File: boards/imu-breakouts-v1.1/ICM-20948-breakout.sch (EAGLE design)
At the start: 10 parts, among them U1 NCP161, U2 ICM-20948

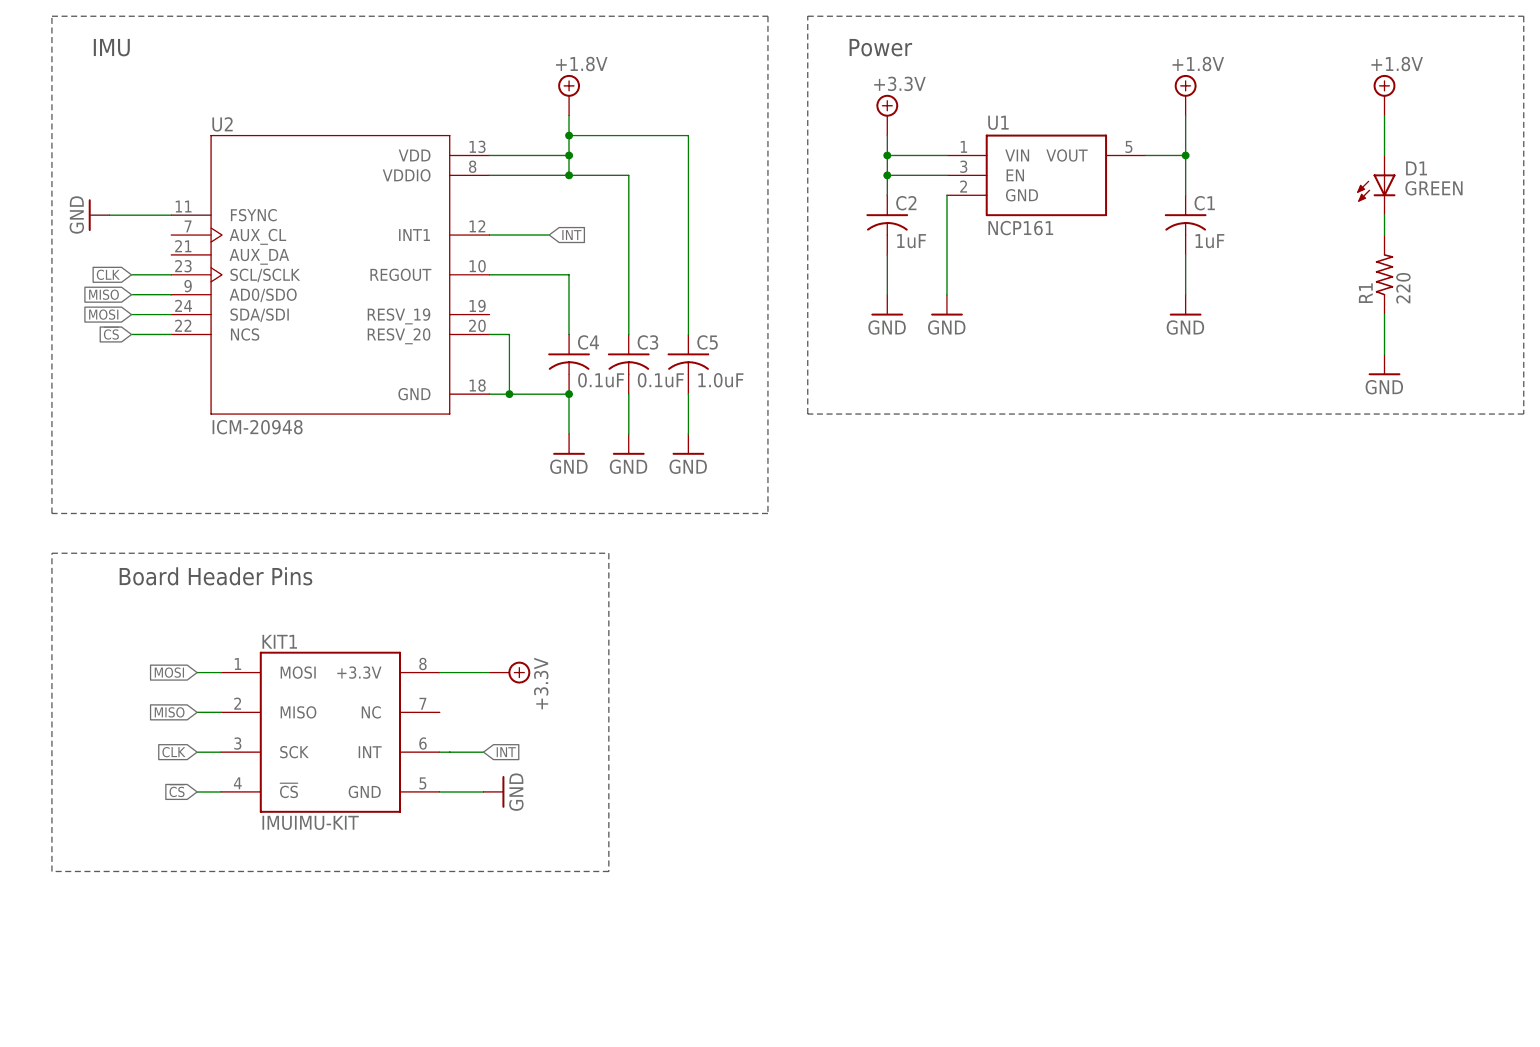
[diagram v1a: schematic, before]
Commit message: Fixed git file locations and version
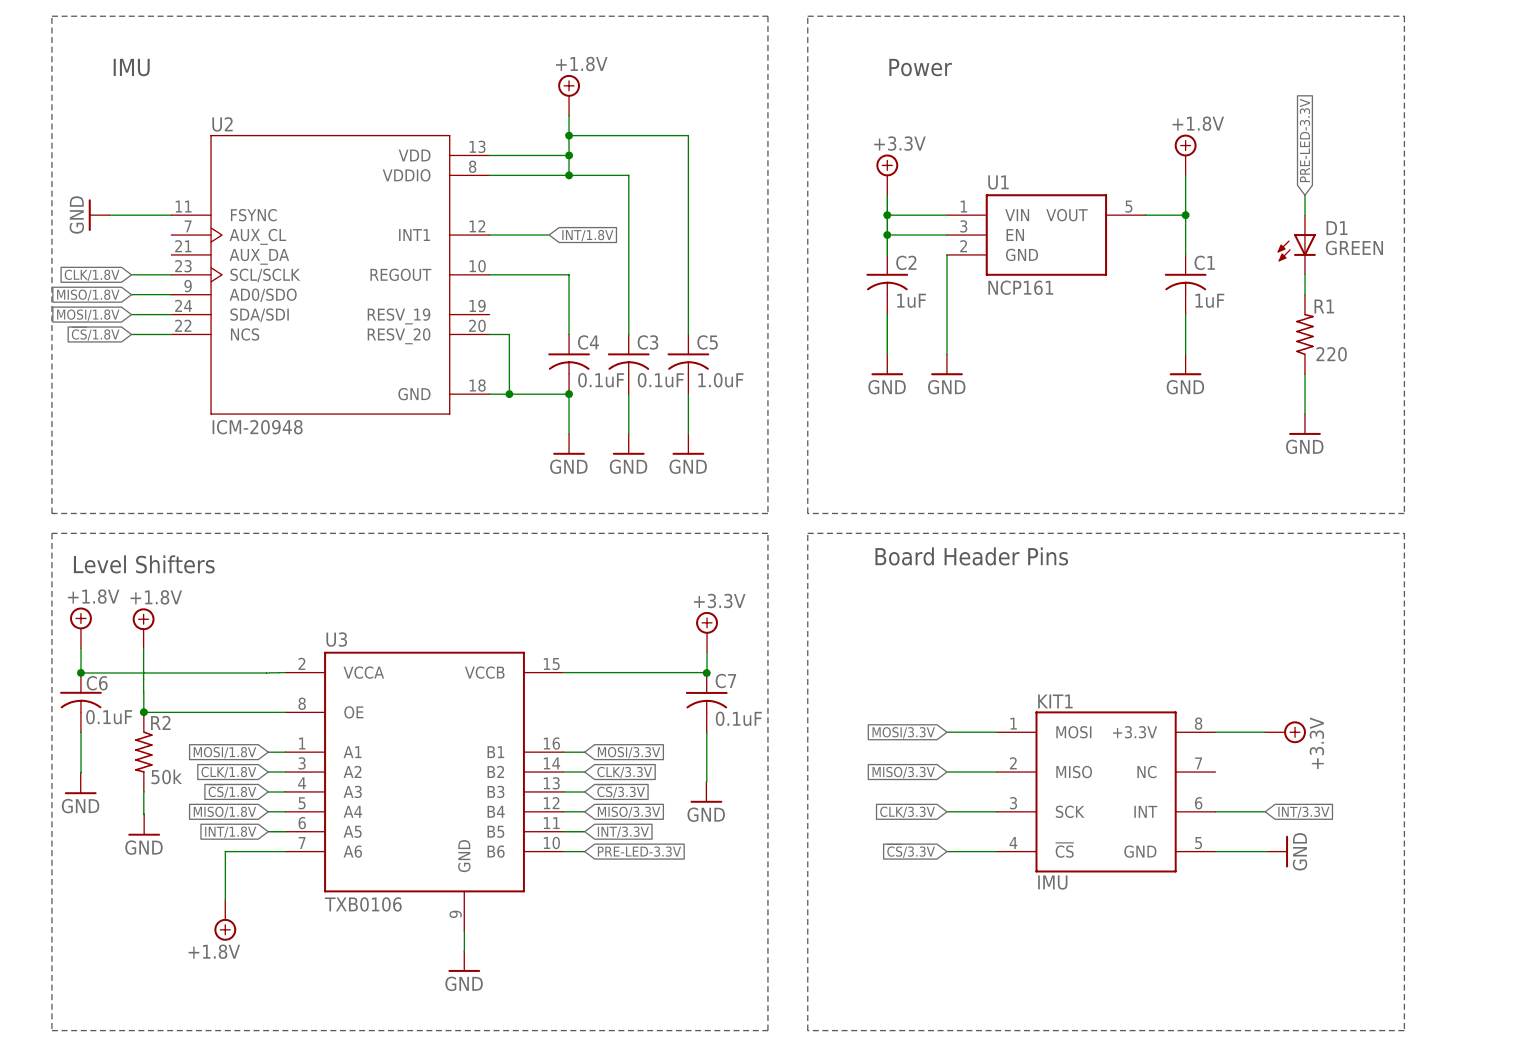
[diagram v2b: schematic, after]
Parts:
- added C6, C7: 0.1uF, rcl:C-USC0603
- added R2: 50k, RoboJackets-Resistors:R0603W
- added U3: TXB0106, TXB0106:TXB0106
- KIT1: value IMUIMU-KIT -> IMU; device RoboJackets-Boards:IMUIMU-KIT -> RoboJackets-Boards:IMU
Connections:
- removed net !CS!: KIT1.!CS!, U2.NCS
- removed net CLK: KIT1.SCK, U2.SCL/SCLK
- removed net INT: KIT1.INT, U2.INT1
- removed net MISO: KIT1.MISO, U2.AD0/SDO
- removed net MOSI: KIT1.MOSI, U2.SDA/SDI
- new net !CS!/1.8V: U2.NCS, U3.A3
- new net !CS!/3.3V: KIT1.!CS!, U3.B3
- new net CLK/1.8V: U2.SCL/SCLK, U3.A2
- new net CLK/3.3V: KIT1.SCK, U3.B2
- new net INT/1.8V: U2.INT1, U3.A5
- new net INT/3.3V: KIT1.INT, U3.B5
- new net MISO/1.8V: U2.AD0/SDO, U3.A4
- new net MISO/3.3V: KIT1.MISO, U3.B4
- new net MOSI/1.8V: U2.SDA/SDI, U3.A1
- new net MOSI/3.3V: KIT1.MOSI, U3.B1
- new net PRE-LED-3.3V: D1.A, U3.B6
- net +1.8V: now also C6.1, R2.PIN1, U3.A6, U3.OE, U3.VCCA; no longer D1.A
- net +3.3V: now also C7.1, U3.VCCB
- net GND: now also C6.2, C7.2, R2.PIN2, U3.GND
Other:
- note added: "Level Shifters"
- moved on the sheet: C1, C2, D1, KIT1, R1, U1
